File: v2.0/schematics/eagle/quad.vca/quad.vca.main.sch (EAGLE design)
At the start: 66 parts, among them IC1 TL084P, IC2 LM13700N, J1 CV2-A, J2 CV1-A, J3 IN-A, J4 OUT-A, J5 CV2-B, J6 CV1-B, J7 IN-B, J8 OUT-B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

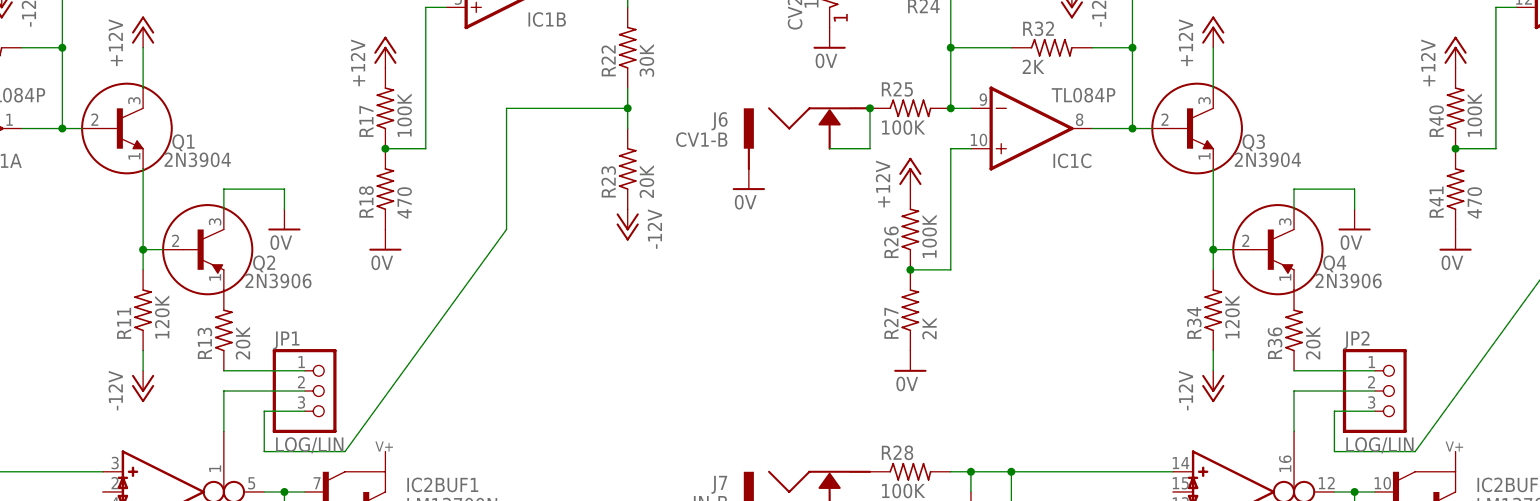
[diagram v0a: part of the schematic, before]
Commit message: Replaced trim pots with tested fixed values. Corrected error in PNP transisitor connection
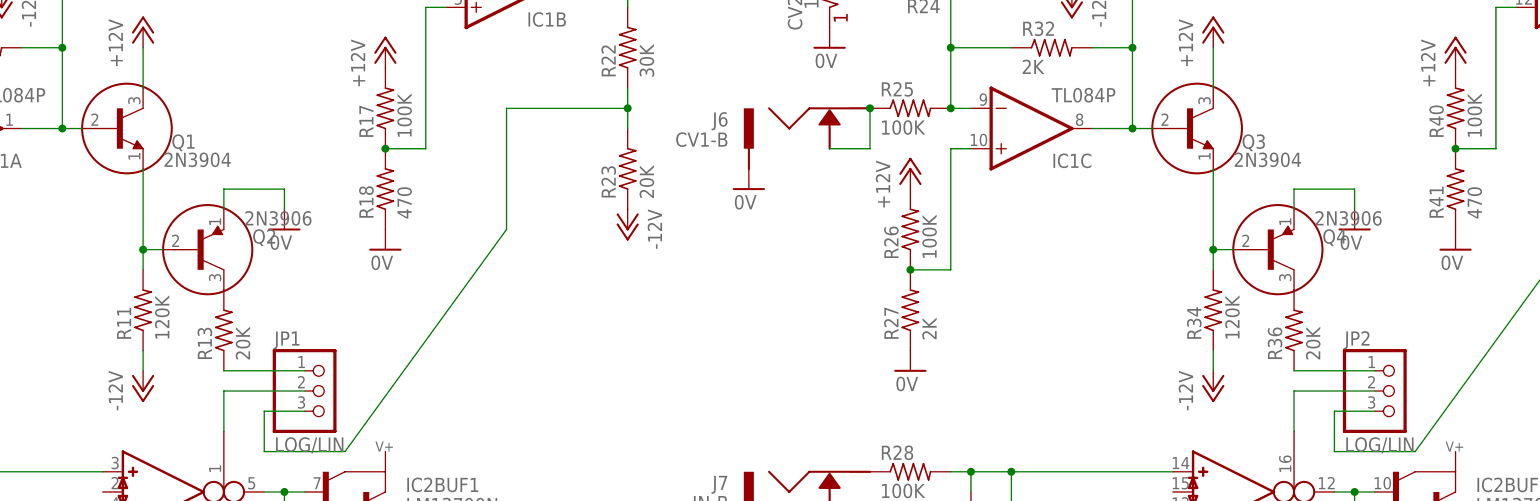
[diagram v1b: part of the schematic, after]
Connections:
- net 0V: now also Q2.E, Q4.E; no longer Q2.C, Q4.C
- net N$30: now also Q4.C; no longer Q4.E
- net N$9: now also Q2.C; no longer Q2.E
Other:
- moved on the sheet: Q2, Q4
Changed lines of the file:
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@@
 <?xml version="1.0" encoding="utf-8"?>
 <!DOCTYPE eagle SYSTEM "eagle.dtd">
-<eagle version="7.2.0">
+<eagle version="7.5.0">
 <drawing>
 <settings>
@@
 <instance part="CVOFFS-A" gate="G$1" x="25.4" y="111.76" rot="R90"/>
 <instance part="BIAS-A" gate="G$1" x="33.02" y="15.24"/>
-<instance part="Q2" gate="G$1" x="50.8" y="71.12"/>
+<instance part="Q2" gate="G$1" x="50.8" y="71.12" rot="MR180"/>
 <instance part="Q1" gate="G$1" x="40.64" y="86.36"/>
 <instance part="IC1" gate="A" x="20.32" y="86.36" rot="MR180"/>
@@
 <instance part="CVOFFS-B" gate="G$1" x="160.02" y="111.76" rot="R90"/>
 <instance part="BIAS-B" gate="G$1" x="167.64" y="15.24"/>
-<instance part="Q4" gate="G$1" x="185.42" y="71.12"/>
+<instance part="Q4" gate="G$1" x="185.42" y="71.12" rot="MR180"/>
 <instance part="Q3" gate="G$1" x="175.26" y="86.36"/>
 <instance part="GND14" gate="1" x="119.38" y="33.02"/>
@@
 </segment>
 <segment>
-<pinref part="Q2" gate="G$1" pin="C"/>
+<pinref part="GND9" gate="1" pin="0V"/>
+<wire x1="60.96" y1="78.74" x2="60.96" y2="76.2" width="0.1524" layer="91"/>
+<pinref part="Q2" gate="G$1" pin="E"/>
 <wire x1="53.34" y1="76.2" x2="53.34" y2="78.74" width="0.1524" layer="91"/>
 <wire x1="53.34" y1="78.74" x2="60.96" y2="78.74" width="0.1524" layer="91"/>
-<pinref part="GND9" gate="1" pin="0V"/>
-<wire x1="60.96" y1="78.74" x2="60.96" y2="76.2" width="0.1524" layer="91"/>
 </segment>
 <segment>
@@
 </segment>
 <segment>
-<pinref part="Q4" gate="G$1" pin="C"/>
+<pinref part="GND20" gate="1" pin="0V"/>
+<wire x1="195.58" y1="78.74" x2="195.58" y2="76.2" width="0.1524" layer="91"/>
+<pinref part="Q4" gate="G$1" pin="E"/>
 <wire x1="187.96" y1="76.2" x2="187.96" y2="78.74" width="0.1524" layer="91"/>
 <wire x1="187.96" y1="78.74" x2="195.58" y2="78.74" width="0.1524" layer="91"/>
-<pinref part="GND20" gate="1" pin="0V"/>
-<wire x1="195.58" y1="78.74" x2="195.58" y2="76.2" width="0.1524" layer="91"/>
 </segment>
 <segment>
@@
 <pinref part="R11" gate="G$1" pin="2"/>
 <wire x1="43.18" y1="81.28" x2="43.18" y2="71.12" width="0.1524" layer="91"/>
-<wire x1="43.18" y1="68.58" x2="43.18" y2="71.12" width="0.1524" layer="91"/>
 <pinref part="Q2" gate="G$1" pin="B"/>
+<wire x1="43.18" y1="71.12" x2="43.18" y2="68.58" width="0.1524" layer="91"/>
 <wire x1="43.18" y1="71.12" x2="45.72" y2="71.12" width="0.1524" layer="91"/>
 <junction x="43.18" y="71.12"/>
-</segment>
-</net>
-<net name="N$9" class="0">
-<segment>
-<pinref part="Q2" gate="G$1" pin="E"/>
-<pinref part="R13" gate="G$1" pin="2"/>
 </segment>
 </net>
@@
 <pinref part="R34" gate="G$1" pin="2"/>
 <wire x1="177.8" y1="81.28" x2="177.8" y2="71.12" width="0.1524" layer="91"/>
-<wire x1="177.8" y1="68.58" x2="177.8" y2="71.12" width="0.1524" layer="91"/>
 <pinref part="Q4" gate="G$1" pin="B"/>
-<wire x1="177.8" y1="71.12" x2="180.34" y2="71.12" width="0.1524" layer="91"/>
+<wire x1="177.8" y1="71.12" x2="177.8" y2="68.58" width="0.1524" layer="91"/>
+<wire x1="180.34" y1="71.12" x2="177.8" y2="71.12" width="0.1524" layer="91"/>
 <junction x="177.8" y="71.12"/>
-</segment>
-</net>
-<net name="N$30" class="0">
-<segment>
-<pinref part="Q4" gate="G$1" pin="E"/>
-<pinref part="R36" gate="G$1" pin="2"/>
 </segment>
 </net>
@@
 </segment>
 </net>
+<net name="N$9" class="0">
+<segment>
+<pinref part="R13" gate="G$1" pin="2"/>
+<pinref part="Q2" gate="G$1" pin="C"/>
+</segment>
+</net>
+<net name="N$30" class="0">
+<segment>
+<pinref part="R36" gate="G$1" pin="2"/>
+<pinref part="Q4" gate="G$1" pin="C"/>
+</segment>
+</net>
